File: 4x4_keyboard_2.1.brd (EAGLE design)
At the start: 69.5 x 142.2 mm, 74 parts, among them U2 AMS1117-5.0

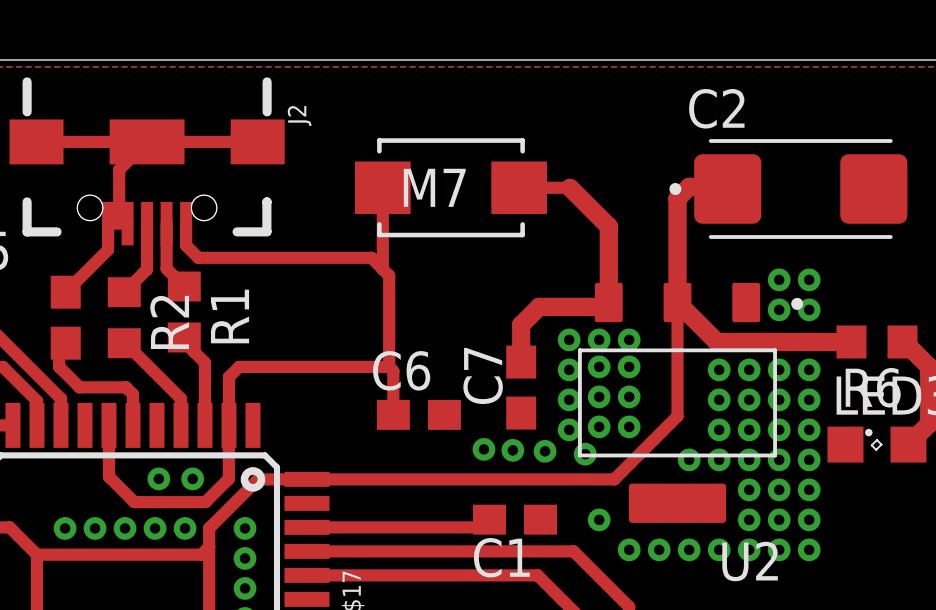
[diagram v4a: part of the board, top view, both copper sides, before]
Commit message: Change forward diode package
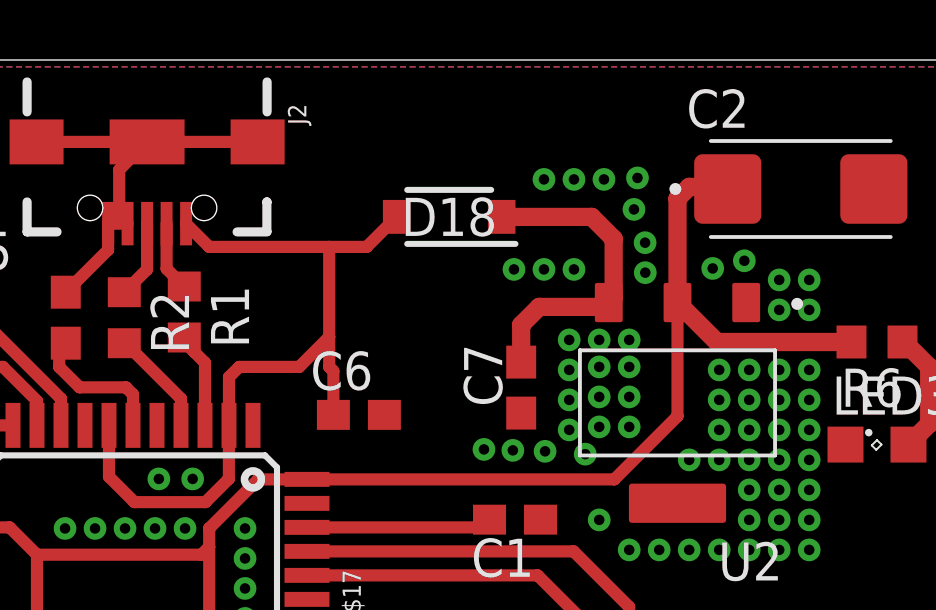
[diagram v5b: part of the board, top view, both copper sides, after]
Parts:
- removed CR1: M7, M7 diode:SMA/DO-214AC_DTC
- added D18: 1N4007W-T, 1N4007W-T:SODFL3818X130N
- moved C6 2.00 mm to (38.0, 130.4)
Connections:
- net N$4: now also D18.1; no longer CR1.2
- net V_USB: now also D18.2; no longer CR1.1
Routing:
- net V_USB: track 30.6 -> 27.1 mm
- net GND: vias 67 -> 79
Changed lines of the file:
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@@
 <drawing>
 <settings>
-<setting alwaysvectorfont="yes"/>
+<setting alwaysvectorfont="no"/>
 <setting keepoldvectorfont="yes"/>
 <setting verticaltext="up"/>
@@
 <attribute name="VALUE" x="26.314" y="134.275" size="1.27" layer="27" rot="R270"/>
 </element>
-<element name="C6" library="rcl" package="C0603" value="1.0uF" x="39.99" y="130.4" smashed="yes" rot="R180">
-<attribute name="NAME" x="38.375" y="131.235" size="1.27" layer="25"/>
-<attribute name="POPULARITY" value="73" x="-7" y="232" size="1.778" layer="27" rot="R180" display="off"/>
-<attribute name="SPICEPREFIX" value="C" x="-7" y="232" size="1.778" layer="27" rot="R180" display="off"/>
-<attribute name="VALUE" x="40.625" y="132.305" size="1.27" layer="27" rot="R180"/>
+<element name="C6" library="rcl" package="C0603" value="1.0uF" x="37.99" y="130.4" smashed="yes" rot="R180">
+<attribute name="NAME" x="36.375" y="131.235" size="1.27" layer="25"/>
+<attribute name="POPULARITY" value="73" x="-9" y="232" size="1.778" layer="27" rot="R180" display="off"/>
+<attribute name="SPICEPREFIX" value="C" x="-9" y="232" size="1.778" layer="27" rot="R180" display="off"/>
+<attribute name="VALUE" x="38.625" y="132.305" size="1.27" layer="27" rot="R180"/>
 </element>
 <element name="C7" library="rcl" package="C0603" value="10uF" x="43.4" y="131.31" smashed="yes" rot="R90">
@@
 <attribute name="SPICEPREFIX" value="C" x="145" y="191" size="1.778" layer="27" rot="R90" display="off"/>
 <attribute name="VALUE" x="45.305" y="130.675" size="1.27" layer="27" rot="R90"/>
-</element>
-<element name="CR1" library="M7 diode" package="SMA/DO-214AC_DTC" value="M7" x="41.06" y="137.97" smashed="yes">
-<attribute name="COPYRIGHT" value="Copyright (C) 2022 Ultra Librarian. All rights reserved." x="69" y="124" size="1.778" layer="27" display="off"/>
-<attribute name="MANUFACTURER_PART_NUMBER" value="M7" x="69" y="124" size="1.778" layer="27" display="off"/>
-<attribute name="MFR_NAME" value="Diotec" x="69" y="124" size="1.778" layer="27" display="off"/>
-<attribute name="NAME" x="37.7834" y="137.335" size="1.27" layer="27" ratio="6" rot="SR0"/>
-<attribute name="VALUE" x="39.3328" y="137.335" size="1.27" layer="21" ratio="6" rot="SR0"/>
 </element>
 <element name="D1" library="1N4148W-13-F" package="SOD3715X135N" value="1N4148W-13-F" x="9.31" y="89.6" smashed="yes">
@@
 <attribute name="RS_PRICE-STOCK" value="http://uk.rs-online.com/web/p/products/7377767P" x="153" y="92" size="1.778" layer="27" display="off"/>
 <attribute name="VALUE" x="58.98" y="101.26" size="1.27" layer="27" align="center"/>
+</element>
+<element name="D18" library="1N4007W-T" package="SODFL3818X130N" value="1N4007W-T" x="41" y="137" smashed="yes" rot="R180">
+<attribute name="ARROW_PART_NUMBER" value="1N4007W-T" x="41" y="137" size="1.778" layer="27" rot="R180" display="off"/>
+<attribute name="ARROW_PRICE-STOCK" value="https://www.arrow.com/en/products/1n4007w-t/rectron?region=nac" x="41" y="137" size="1.778" layer="27" rot="R180" display="off"/>
+<attribute name="DESCRIPTION" value="Rectifiers SOD-123,1A,1000V,GP" x="41" y="137" size="1.778" layer="27" rot="R180" display="off"/>
+<attribute name="HEIGHT" value="1.3mm" x="41" y="137" size="1.778" layer="27" rot="R180" display="off"/>
+<attribute name="MANUFACTURER_NAME" value="Rectron" x="41" y="137" size="1.778" layer="27" rot="R180" display="off"/>
+<attribute name="MANUFACTURER_PART_NUMBER" value="1N4007W-T" x="41" y="137" size="1.778" layer="27" rot="R180" display="off"/>
+<attribute name="MOUSER_PART_NUMBER" value="583-1N4007W-T" x="41" y="137" size="1.778" layer="27" rot="R180" display="off"/>
+<attribute name="MOUSER_PRICE-STOCK" value="https://www.mouser.co.uk/ProductDetail/Rectron/1N4007W-T?qs=QNEnbhJQKvah3J4JbJr%2FPw%3D%3D" x="41" y="137" size="1.778" layer="27" rot="R180" display="off"/>
+<attribute name="NAME" x="41" y="137" size="1.27" layer="25" rot="R180" align="center"/>
+<attribute name="VALUE" x="41" y="137" size="1.27" layer="27" rot="R180" align="center"/>
 </element>
 </elements>
@@
 <via x="31.195" y="126.615" extent="1-16" drill="0.35"/>
 <via x="32.195" y="126.615" extent="1-16" drill="0.35"/>
+<via x="45.159" y="135.25" extent="1-16" drill="0.35"/>
+<via x="44.159" y="135.25" extent="1-16" drill="0.35"/>
+<via x="43.159" y="135.25" extent="1-16" drill="0.35"/>
+<via x="47.159" y="137.25" extent="1-16" drill="0.35"/>
+<via x="46.159" y="138.25" extent="1-16" drill="0.35"/>
+<via x="44.159" y="138.25" extent="1-16" drill="0.35"/>
+<via x="45.159" y="138.25" extent="1-16" drill="0.35"/>
+<via x="49.784" y="135.282" extent="1-16" drill="0.35"/>
+<via x="50.838" y="135.537" extent="1-16" drill="0.35"/>
+<via x="47.53" y="136.14" extent="1-16" drill="0.35"/>
+<via x="47.536" y="135.141" extent="1-16" drill="0.35"/>
+<via x="47.276" y="138.299" extent="1-16" drill="0.35"/>
 </signal>
 <signal name="D-">
@@
 <contactref element="C6" pad="2"/>
 <contactref element="J2" pad="VBUS"/>
-<contactref element="CR1" pad="1"/>
 <contactref element="U$17" pad="2"/>
 <contactref element="U$17" pad="7"/>
@@
 <wire x1="33.655" y1="128.27" x2="33.655" y2="130.045" width="0.4064" layer="1"/>
 <wire x1="33.655" y1="130.045" x2="33.66" y2="130.05" width="0.4064" layer="1"/>
-<wire x1="39.14" y1="130.4" x2="39.14" y2="131.86" width="0.4064" layer="1"/>
-<wire x1="39.14" y1="131.86" x2="39" y2="132" width="0.4064" layer="1"/>
+<contactref element="D18" pad="2"/>
+<wire x1="32.23" y1="136.775" x2="32.23" y2="136.77" width="0.4064" layer="1"/>
+<wire x1="32.23" y1="136.77" x2="33" y2="136" width="0.4064" layer="1"/>
+<wire x1="33" y1="136" x2="37" y2="136" width="0.4064" layer="1"/>
+<wire x1="37" y1="136" x2="38.25" y2="136" width="0.4064" layer="1"/>
+<wire x1="38.25" y1="136" x2="39.25" y2="137" width="0.4064" layer="1"/>
 <wire x1="33.66" y1="130.05" x2="33.66" y2="131.66" width="0.4064" layer="1"/>
 <wire x1="33.66" y1="131.66" x2="34" y2="132" width="0.4064" layer="1"/>
-<wire x1="34" y1="132" x2="39" y2="132" width="0.4064" layer="1"/>
-<wire x1="32.23" y1="136.775" x2="32.23" y2="136.045" width="0.4064" layer="1"/>
-<wire x1="32.23" y1="136.045" x2="32.639" y2="135.636" width="0.4064" layer="1"/>
-<wire x1="32.639" y1="135.636" x2="38.4057" y2="135.636" width="0.4064" layer="1"/>
-<wire x1="38.4057" y1="135.636" x2="38.7867" y2="135.255" width="0.4064" layer="1"/>
-<wire x1="39" y1="135.0417" x2="39" y2="132" width="0.4064" layer="1"/>
-<wire x1="38.7867" y1="137.97" x2="38.7867" y2="135.255" width="0.4064" layer="1"/>
-<wire x1="38.7867" y1="135.255" x2="39" y2="135.0417" width="0.4064" layer="1"/>
+<wire x1="34" y1="132" x2="36" y2="132" width="0.4064" layer="1"/>
+<wire x1="37" y1="133" x2="37" y2="136" width="0.4064" layer="1"/>
+<wire x1="36" y1="132" x2="37" y2="133" width="0.4064" layer="1"/>
+<wire x1="37.14" y1="130.4" x2="37.14" y2="131.86" width="0.4064" layer="1"/>
+<wire x1="37.14" y1="131.86" x2="37" y2="132" width="0.4064" layer="1"/>
+<wire x1="37" y1="132" x2="37" y2="133" width="0.4064" layer="1"/>
 </signal>
 <signal name="VCC">
@@
 <signal name="N$4">
 <contactref element="U2" pad="3"/>
-<contactref element="CR1" pad="2"/>
 <contactref element="C7" pad="2"/>
-<wire x1="45.03" y1="137.97" x2="46.32" y2="136.68" width="0.6096" layer="1"/>
-<wire x1="46.32" y1="134.145" x2="46.32" y2="136.68" width="0.6096" layer="1"/>
 <wire x1="43.4" y1="132.16" x2="43.4" y2="133.4" width="0.6096" layer="1"/>
 <wire x1="43.4" y1="133.4" x2="44" y2="134" width="0.6096" layer="1"/>
 <wire x1="44" y1="134" x2="46.175" y2="134" width="0.6096" layer="1"/>
 <wire x1="46.175" y1="134" x2="46.32" y2="134.145" width="0.6096" layer="1"/>
-<wire x1="43.3333" y1="137.97" x2="45.03" y2="137.97" width="0.4064" layer="1"/>
+<contactref element="D18" pad="1"/>
+<wire x1="42.75" y1="137" x2="45.753" y2="137" width="0.6096" layer="1"/>
+<wire x1="45.753" y1="137" x2="46.482" y2="136.271" width="0.6096" layer="1"/>
+<wire x1="46.482" y1="136.271" x2="46.482" y2="134.307" width="0.6096" layer="1"/>
+<wire x1="46.482" y1="134.307" x2="46.32" y2="134.145" width="0.6096" layer="1"/>
 </signal>
 </signals>

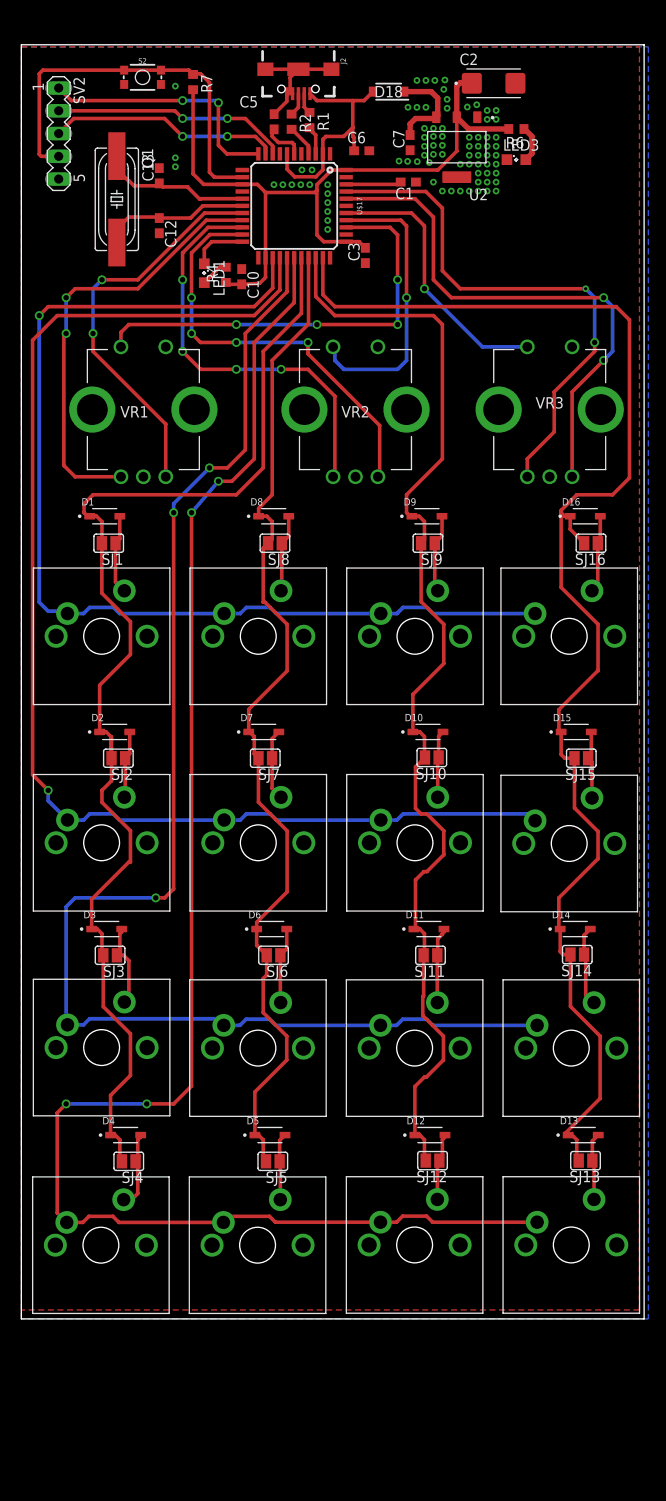
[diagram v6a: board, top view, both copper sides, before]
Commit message: Added the usb c and usb A package
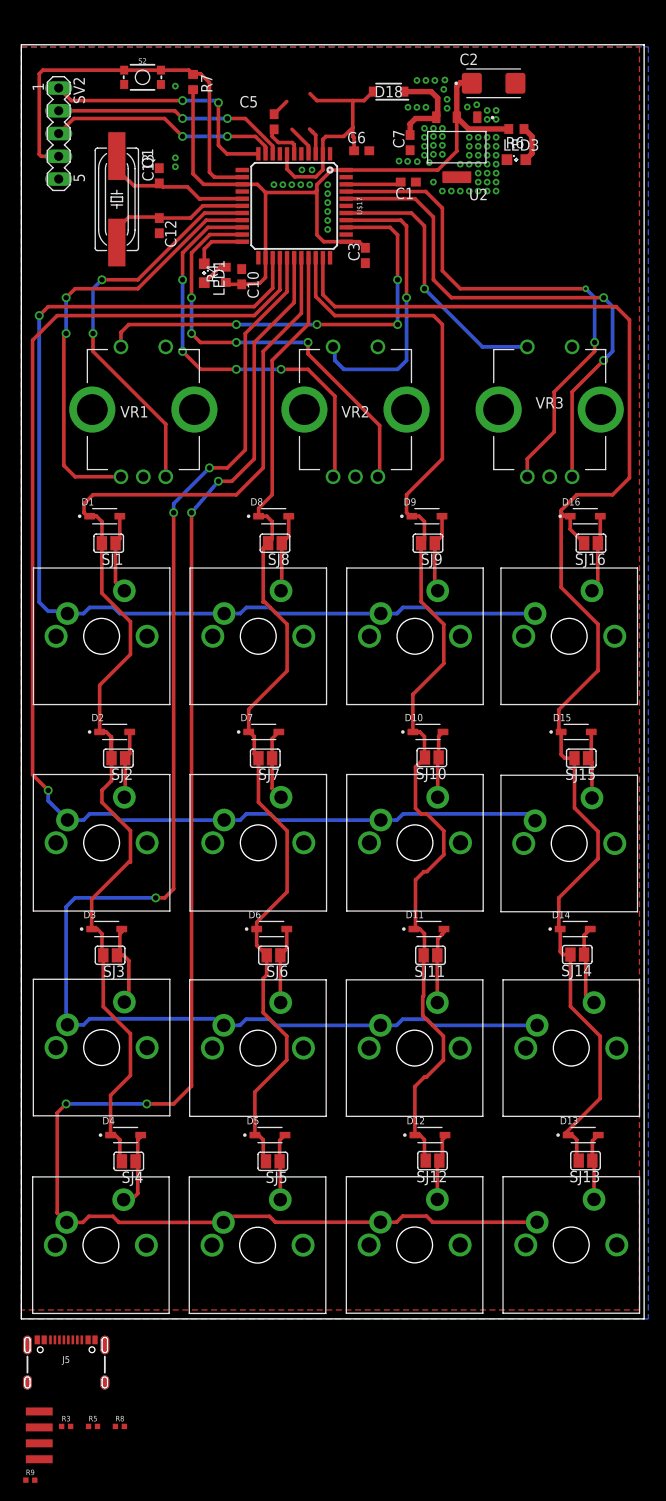
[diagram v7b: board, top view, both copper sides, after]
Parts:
- removed J2: (no value), SparkFun-Connectors:USB-B-MICRO-SMD
- removed R1, R2: 22, audio amplifier example:R0603
- added J5: (no value), USBC:USB-C-16P-5
- added JP14: USB_SOLDER_PADS, SparkFun-Connectors:USB-SOLDER-PADS
- added R3, R5, R8, R9: 5.1k, SparkFun-Resistors:0402-TIGHT
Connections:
- removed net N$1: J2.D-, R1.1
- removed net N$3: J2.D+, R2.1
- new net D-_HV: J5.A7, J5.B7, JP14.D-, R8.1
- new net DP_HV: J5.A6, J5.B6, JP14.D+, R9.1
- new net N$13: J5.B5, R3.2
- new net N$7: J5.A5, R5.2
- net D+: now also R9.2; no longer R2.2
- net D-: now also R8.2; no longer R1.2
- net GND: now also J5.GND, J5.GND2, JP14.GND, R3.1, R5.1; no longer J2.GND, J2.ID, J2.SHIELD1, J2.SHIELD2, J2.SHIELD3
- net V_USB: now also J5.VBUS1, J5.VBUS2, JP14.VBUS; no longer J2.VBUS
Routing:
- net GND: track 14.2 -> 2.00 mm
- net N$3: track 2.60 -> 0.00 mm
- net N$1: track 2.34 -> 0.00 mm
